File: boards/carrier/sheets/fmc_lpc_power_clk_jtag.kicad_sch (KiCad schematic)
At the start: 1 part, among them J4C FX10A-168P-SV(91)

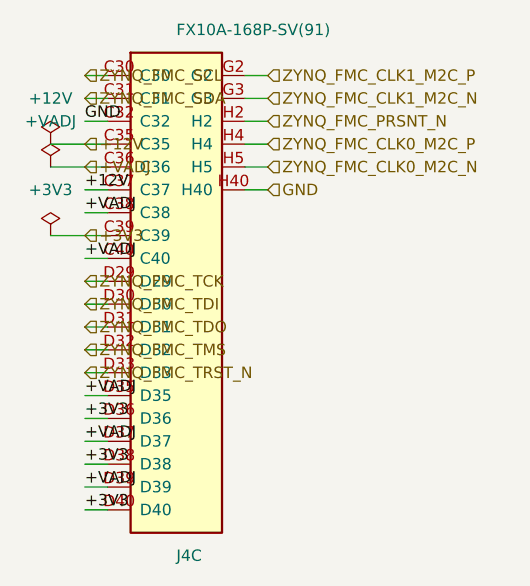
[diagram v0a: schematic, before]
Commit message: symbols: hide pin names on dense connectors + widen FUSB302 cap pitch
Three visual fixes from PDF page-level review:

1. FX10A bank symbols (som_j*, fmc_lpc_*): switch show_pin_names
   True → False in connector_bank_symbols.py. Pin NAMES were
   overlapping pin NUMBERS at the pin position.

2. USBC_16P symbol: add (pin_names (hide yes)) — KiCad defaulted to
   visible, causing GND/VBUS/CC1/D+/D-/... text to overlap pin
   numbers A1/A4/A5/A6/... at 2.54mm pin pitch.

3. FUSB302 refcircuit: dense_swarm=True so the 15 external_parts
   across 7 pins (multi-cap decoupling on VDD/VBUS/VCONN) use the
   20.32mm dense pitch — value labels stop overlapping between
   adjacent slot columns.

Final: 0 ERC errors, 486 warnings, 28-page A3 PDF, 90/90 tests.
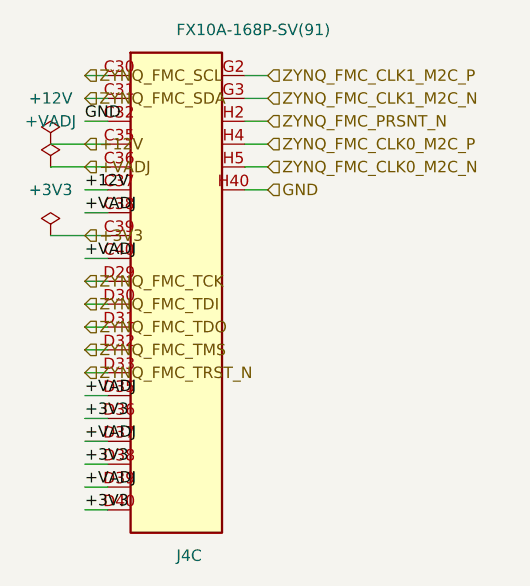
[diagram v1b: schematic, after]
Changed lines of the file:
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@@
 		(instances
 			(project "FMC LPC bank C (power + clock + JTAG + mgmt)"
-				(path "/87960743-179f-4487-8f3e-6ad564735a97"
+				(path "/c5e0cfad-5336-4d37-921e-85973cb428b0"
 					(reference "J4C")
 					(unit 1)
@@
 		(instances
 			(project "FMC LPC bank C (power + clock + JTAG + mgmt)"
-				(path "/87960743-179f-4487-8f3e-6ad564735a97"
+				(path "/c5e0cfad-5336-4d37-921e-85973cb428b0"
 					(reference "#FLG100")
 					(unit 1)
@@
 		(instances
 			(project "FMC LPC bank C (power + clock + JTAG + mgmt)"
-				(path "/87960743-179f-4487-8f3e-6ad564735a97"
+				(path "/c5e0cfad-5336-4d37-921e-85973cb428b0"
 					(reference "#FLG101")
 					(unit 1)
@@
 		(instances
 			(project "FMC LPC bank C (power + clock + JTAG + mgmt)"
-				(path "/87960743-179f-4487-8f3e-6ad564735a97"
+				(path "/c5e0cfad-5336-4d37-921e-85973cb428b0"
 					(reference "#FLG102")
 					(unit 1)
